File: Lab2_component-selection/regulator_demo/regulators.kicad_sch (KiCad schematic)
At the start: 23 parts, among them J1 n.m., J2 n.m., J3 n.m., J4 n.m., U1 LM317_SOT-223, U2 TPS79301-EP, U3 MIC5377

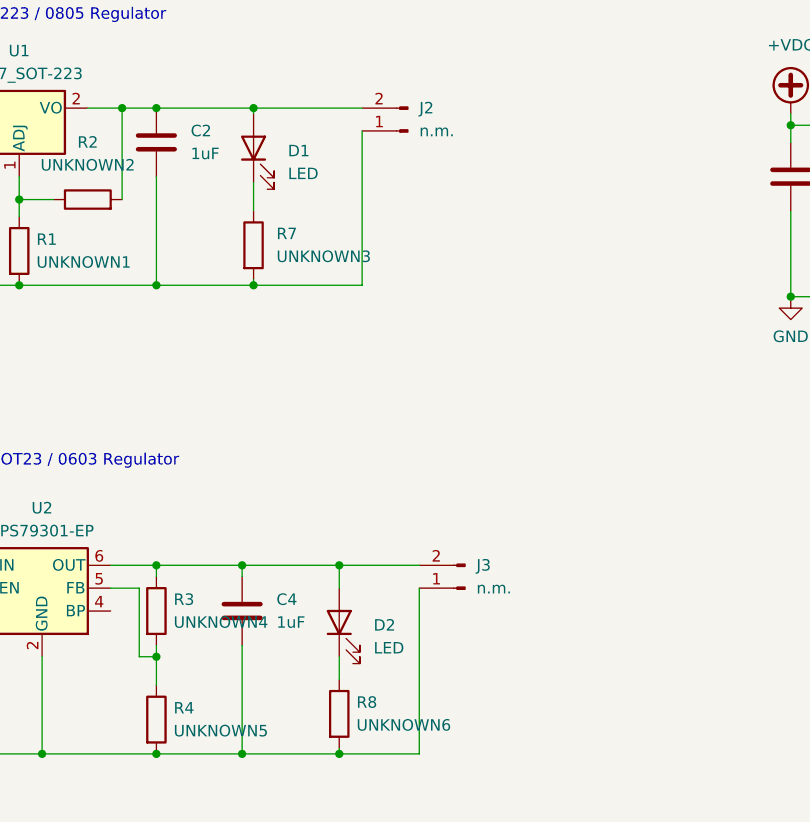
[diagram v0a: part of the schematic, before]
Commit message: updated schematic values for LEDs
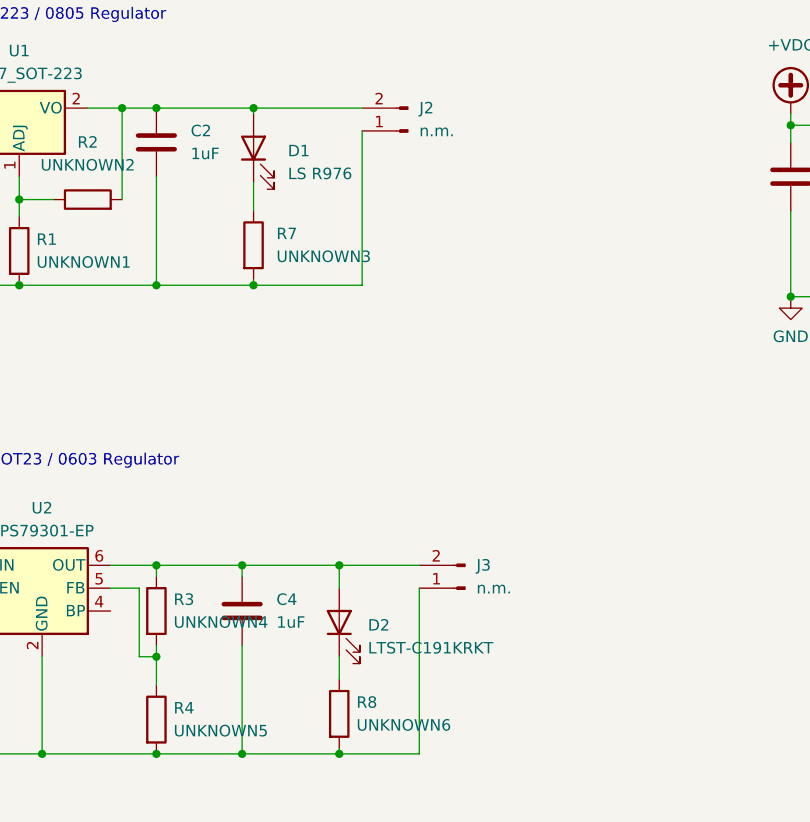
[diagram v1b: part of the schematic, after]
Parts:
- D1: value LED -> LS R976
- D2: value LED -> LTST-C191KRKT
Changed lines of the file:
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@@
       (effects (font (size 1.27 1.27)) (justify right))
     )
-    (property "Value" "LED" (at 78.74 63.1825 90)
+    (property "Value" "LS R976" (at 78.74 63.1825 90)
       (effects (font (size 1.27 1.27)) (justify right))
     )
@@
   (symbol (lib_id "Device:LED") (at 84.455 113.03 90) (unit 1)
     (in_bom yes) (on_board yes) (dnp no) (fields_autoplaced)
-    (property "Reference" "D2" (at 88.265 113.3475 90)
-      (effects (font (size 1.27 1.27)) (justify right))
-    )
-    (property "Value" "LED" (at 88.265 115.8875 90)
-      (effects (font (size 1.27 1.27)) (justify right))
-    )
+    (property "Reference" "D2" (at 87.63 113.3475 90)
+      (effects (font (size 1.27 1.27)) (justify right))
+    )
+    (property "Value" "LTST-C191KRKT" (at 87.63 115.8875 90)
+      (effects (font (size 1.27 1.27)) (justify right))
+    )
